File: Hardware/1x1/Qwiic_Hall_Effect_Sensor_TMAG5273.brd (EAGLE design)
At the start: 25.4 x 25.4 mm, 51 parts, among them J1 QWIIC_RIGHT_ANGLE, J2 QWIIC_RIGHT_ANGLE, Q1 20V/4.2A/52mΩ/1.4W, U1 TMAG5273

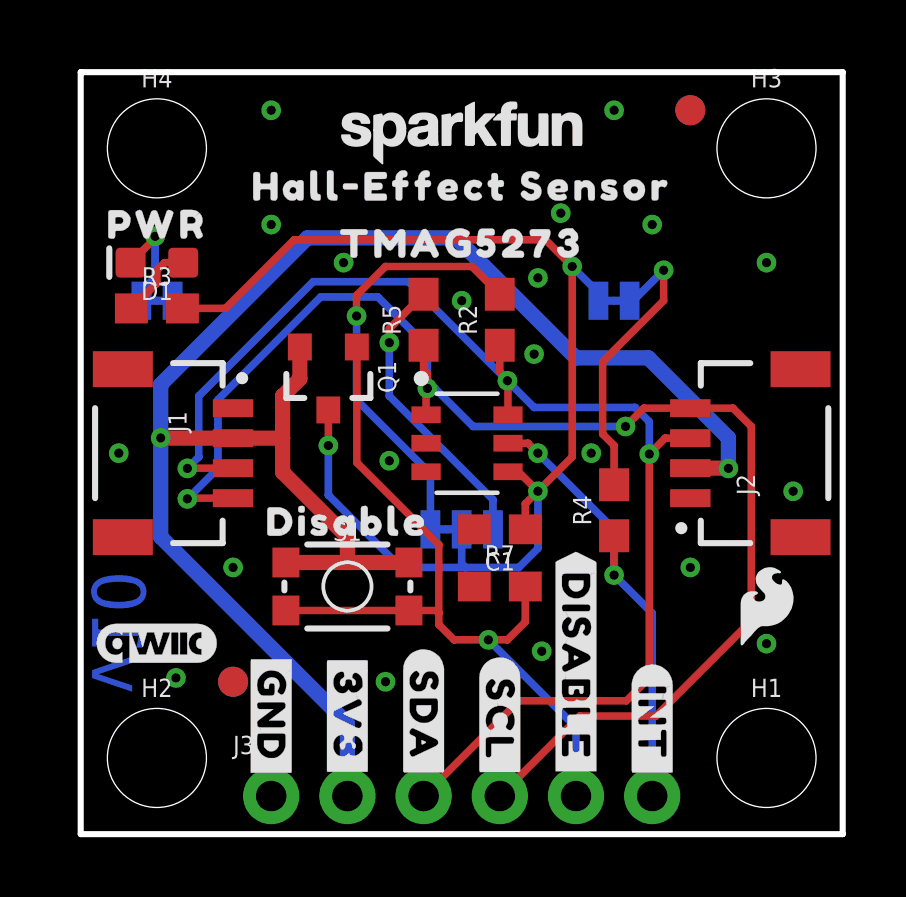
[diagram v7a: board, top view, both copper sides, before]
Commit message: Files for ordering
Re-added the correct panel files for the project along with ordering instructions. Made final adjustments from design review and board is ready for order!
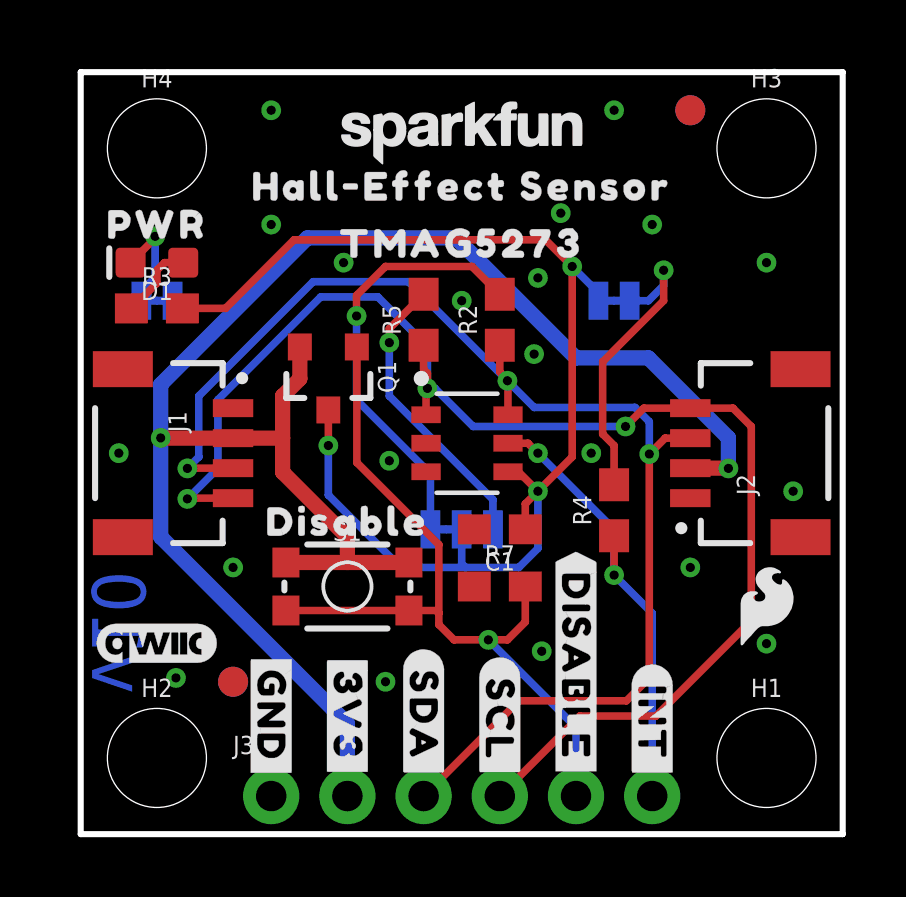
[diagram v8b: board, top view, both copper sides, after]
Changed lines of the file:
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@@
 <drawing>
 <settings>
-<setting alwaysvectorfont="yes"/>
+<setting alwaysvectorfont="no"/>
 <setting verticaltext="up"/>
 </settings>
@@
 <layer number="23" name="tOrigins" color="15" fill="1" visible="yes" active="yes"/>
 <layer number="24" name="bOrigins" color="15" fill="1" visible="yes" active="yes"/>
-<layer number="25" name="tNames" color="7" fill="1" visible="no" active="yes"/>
-<layer number="26" name="bNames" color="7" fill="1" visible="no" active="yes"/>
-<layer number="27" name="tValues" color="7" fill="1" visible="no" active="yes"/>
-<layer number="28" name="bValues" color="7" fill="1" visible="no" active="yes"/>
-<layer number="29" name="tStop" color="7" fill="3" visible="no" active="yes"/>
-<layer number="30" name="bStop" color="7" fill="6" visible="no" active="yes"/>
-<layer number="31" name="tCream" color="7" fill="4" visible="no" active="yes"/>
-<layer number="32" name="bCream" color="7" fill="5" visible="no" active="yes"/>
-<layer number="33" name="tFinish" color="6" fill="3" visible="no" active="yes"/>
-<layer number="34" name="bFinish" color="6" fill="6" visible="no" active="yes"/>
-<layer number="35" name="tGlue" color="7" fill="4" visible="no" active="yes"/>
-<layer number="36" name="bGlue" color="7" fill="5" visible="no" active="yes"/>
-<layer number="37" name="tTest" color="7" fill="1" visible="no" active="yes"/>
-<layer number="38" name="bTest" color="7" fill="1" visible="no" active="yes"/>
-<layer number="39" name="tKeepout" color="4" fill="11" visible="no" active="yes"/>
-<layer number="40" name="bKeepout" color="1" fill="11" visible="no" active="yes"/>
-<layer number="41" name="tRestrict" color="4" fill="10" visible="no" active="yes"/>
-<layer number="42" name="bRestrict" color="1" fill="10" visible="no" active="yes"/>
-<layer number="43" name="vRestrict" color="2" fill="10" visible="no" active="yes"/>
-<layer number="44" name="Drills" color="7" fill="1" visible="no" active="yes"/>
+<layer number="25" name="tNames" color="7" fill="1" visible="yes" active="yes"/>
+<layer number="26" name="bNames" color="7" fill="1" visible="yes" active="yes"/>
+<layer number="27" name="tValues" color="7" fill="1" visible="yes" active="yes"/>
+<layer number="28" name="bValues" color="7" fill="1" visible="yes" active="yes"/>
+<layer number="29" name="tStop" color="7" fill="3" visible="yes" active="yes"/>
+<layer number="30" name="bStop" color="7" fill="6" visible="yes" active="yes"/>
+<layer number="31" name="tCream" color="7" fill="4" visible="yes" active="yes"/>
+<layer number="32" name="bCream" color="7" fill="5" visible="yes" active="yes"/>
+<layer number="33" name="tFinish" color="6" fill="3" visible="yes" active="yes"/>
+<layer number="34" name="bFinish" color="6" fill="6" visible="yes" active="yes"/>
+<layer number="35" name="tGlue" color="7" fill="4" visible="yes" active="yes"/>
+<layer number="36" name="bGlue" color="7" fill="5" visible="yes" active="yes"/>
+<layer number="37" name="tTest" color="7" fill="1" visible="yes" active="yes"/>
+<layer number="38" name="bTest" color="7" fill="1" visible="yes" active="yes"/>
+<layer number="39" name="tKeepout" color="4" fill="11" visible="yes" active="yes"/>
+<layer number="40" name="bKeepout" color="1" fill="11" visible="yes" active="yes"/>
+<layer number="41" name="tRestrict" color="4" fill="10" visible="yes" active="yes"/>
+<layer number="42" name="bRestrict" color="1" fill="10" visible="yes" active="yes"/>
+<layer number="43" name="vRestrict" color="2" fill="10" visible="yes" active="yes"/>
+<layer number="44" name="Drills" color="7" fill="1" visible="yes" active="yes"/>
 <layer number="45" name="Holes" color="7" fill="1" visible="yes" active="yes"/>
-<layer number="46" name="Milling" color="3" fill="1" visible="no" active="yes"/>
-<layer number="47" name="Measures" color="7" fill="1" visible="no" active="yes"/>
-<layer number="48" name="Document" color="7" fill="1" visible="no" active="yes"/>
-<layer number="49" name="Reference" color="7" fill="1" visible="no" active="yes"/>
+<layer number="46" name="Milling" color="3" fill="1" visible="yes" active="yes"/>
+<layer number="47" name="Measures" color="7" fill="1" visible="yes" active="yes"/>
+<layer number="48" name="Document" color="7" fill="1" visible="yes" active="yes"/>
+<layer number="49" name="Reference" color="7" fill="1" visible="yes" active="yes"/>
 <layer number="50" name="dxf" color="7" fill="1" visible="no" active="no"/>
 <layer number="51" name="tDocu" color="6" fill="1" visible="yes" active="yes"/>
-<layer number="52" name="bDocu" color="7" fill="1" visible="no" active="yes"/>
+<layer number="52" name="bDocu" color="7" fill="1" visible="yes" active="yes"/>
 <layer number="53" name="tGND_GNDA" color="7" fill="9" visible="no" active="no"/>
 <layer number="54" name="bGND_GNDA" color="1" fill="9" visible="no" active="no"/>
@@
 <contactref element="JP2" pad="1"/>
 <contactref element="R4" pad="2"/>
-<wire x1="18.3007" y1="17.78" x2="18.415" y2="17.78" width="0.254" layer="16"/>
-<wire x1="19.431" y1="18.796" x2="18.415" y2="17.78" width="0.254" layer="16"/>
+<wire x1="18.3007" y1="17.78" x2="18.923" y2="17.78" width="0.254" layer="16"/>
+<wire x1="19.431" y1="18.796" x2="19.431" y2="18.288" width="0.254" layer="16"/>
+<wire x1="19.431" y1="18.288" x2="18.923" y2="17.78" width="0.254" layer="16"/>
 <via x="19.431" y="18.796" extent="1-16" drill="0.3048"/>
 <wire x1="19.431" y1="18.796" x2="19.431" y2="17.78" width="0.254" layer="1"/>
